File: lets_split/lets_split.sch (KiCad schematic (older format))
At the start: 56 parts, among them P1 USB-rewire, P2 USB_OTG, P3 WS2812-Strip, P4 TRRS jack, SW1 SW_PUSH, SW10 SW_PUSH, SW11 SW_PUSH, SW12 SW_PUSH, SW13 SW_PUSH, SW14 SW_PUSH, SW15 SW_PUSH, SW16 SW_PUSH, SW17 SW_PUSH, SW18 SW_PUSH, SW19 SW_PUSH, SW2 SW_PUSH, SW20 SW_PUSH, SW21 SW_PUSH, SW22 SW_PUSH, SW23 SW_PUSH, SW24 SW_PUSH, SW3 SW_PUSH, SW4 SW_PUSH, SW5 SW_PUSH, SW6 SW_PUSH, SW7 SW_PUSH, SW8 SW_PUSH, SW9 SW_PUSH, U1 ArduinoProMicro

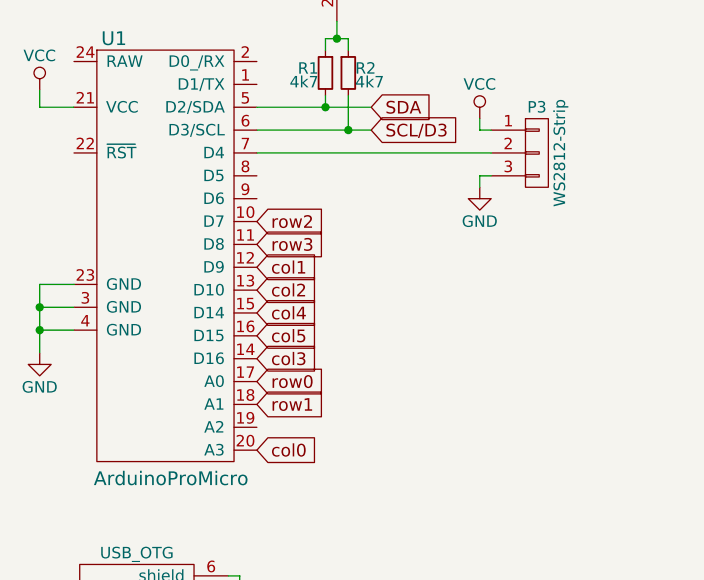
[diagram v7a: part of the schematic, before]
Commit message: Routed board with reversible socket footprint, and mirrored connectors
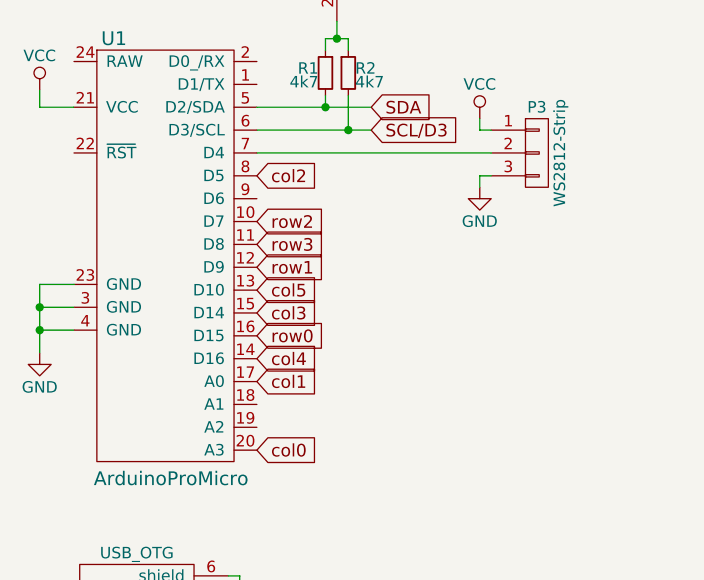
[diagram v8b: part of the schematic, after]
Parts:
- SW1, SW10, SW11, SW12, SW13, SW14, SW15, SW16, SW17, SW18, SW19, SW2, SW20, SW21, SW22, SW23, SW24, SW3, SW4, SW5, SW6, SW7, SW8, SW9: footprint CherryMX:Kailh-socket -> CherryMX:Kailh-socket-mirrorable
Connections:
- net col1: now also U1.17 (A0); no longer U1.12 (D9)
- net col2: now also U1.8 (D5); no longer U1.13 (D10)
- net col3: now also U1.15 (D14); no longer U1.14 (D16)
- net col4: now also U1.14 (D16); no longer U1.15 (D14)
- net col5: now also U1.13 (D10); no longer U1.16 (D15)
- net row0: now also U1.16 (D15); no longer U1.17 (A0)
- net row1: now also U1.12 (D9); no longer U1.18 (A1)
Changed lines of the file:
@@
-EESchema Schematic File Version 2
+EESchema Schematic File Version 3
 LIBS:power
 LIBS:device
-LIBS:transistors
-LIBS:conn
 LIBS:linear
 LIBS:regul
-LIBS:74xx
-LIBS:cmos4000
 LIBS:adc-dac
 LIBS:memory
@@
 LIBS:digital-audio
 LIBS:philips
-LIBS:display
 LIBS:cypress
 LIBS:siliconi
@@
 LIBS:atmel
 LIBS:contrib
-LIBS:valves
 LIBS:8Bit-MCU
 LIBS:lets_split-cache
-EELAYER 25 0
+EELAYER 26 0
 EELAYER END
 $Descr A4 11693 8268
@@
 F 0 "SW1" H 5600 2310 50  0000 C CNN
 F 1 "SW_PUSH" H 5450 2120 50  0000 C CNN
-F 2 "CherryMX:Kailh-socket" H 5450 2200 50  0001 C CNN
+F 2 "CherryMX:Kailh-socket-mirrorable" H 5450 2200 50  0001 C CNN
 F 3 "" H 5450 2200 50  0000 C CNN
 	1    5450 2200
@@
 F 0 "SW2" H 6350 2310 50  0000 C CNN
 F 1 "SW_PUSH" H 6200 2120 50  0000 C CNN
-F 2 "CherryMX:Kailh-socket" H 6200 2200 50  0001 C CNN
+F 2 "CherryMX:Kailh-socket-mirrorable" H 6200 2200 50  0001 C CNN
 F 3 "" H 6200 2200 50  0000 C CNN
 	1    6200 2200
@@
 F 0 "SW3" H 7050 2310 50  0000 C CNN
 F 1 "SW_PUSH" H 6900 2120 50  0000 C CNN
-F 2 "CherryMX:Kailh-socket" H 6900 2200 50  0001 C CNN
+F 2 "CherryMX:Kailh-socket-mirrorable" H 6900 2200 50  0001 C CNN
 F 3 "" H 6900 2200 50  0000 C CNN
 	1    6900 2200
@@
 F 0 "SW4" H 7800 2310 50  0000 C CNN
 F 1 "SW_PUSH" H 7650 2120 50  0000 C CNN
-F 2 "CherryMX:Kailh-socket" H 7650 2200 50  0001 C CNN
+F 2 "CherryMX:Kailh-socket-mirrorable" H 7650 2200 50  0001 C CNN
 F 3 "" H 7650 2200 50  0000 C CNN
 	1    7650 2200
@@
 F 0 "SW5" H 8550 2310 50  0000 C CNN
 F 1 "SW_PUSH" H 8400 2120 50  0000 C CNN
-F 2 "CherryMX:Kailh-socket" H 8400 2200 50  0001 C CNN
+F 2 "CherryMX:Kailh-socket-mirrorable" H 8400 2200 50  0001 C CNN
 F 3 "" H 8400 2200 50  0000 C CNN
 	1    8400 2200
@@
 F 0 "SW6" H 9300 2310 50  0000 C CNN
 F 1 "SW_PUSH" H 9150 2120 50  0000 C CNN
-F 2 "CherryMX:Kailh-socket" H 9150 2200 50  0001 C CNN
+F 2 "CherryMX:Kailh-socket-mirrorable" H 9150 2200 50  0001 C CNN
 F 3 "" H 9150 2200 50  0000 C CNN
 	1    9150 2200
@@
 F 0 "SW7" H 5600 2810 50  0000 C CNN
 F 1 "SW_PUSH" H 5450 2620 50  0000 C CNN
-F 2 "CherryMX:Kailh-socket" H 5450 2700 50  0001 C CNN
+F 2 "CherryMX:Kailh-socket-mirrorable" H 5450 2700 50  0001 C CNN
 F 3 "" H 5450 2700 50  0000 C CNN
 	1    5450 2700
@@
 F 0 "SW8" H 6350 2810 50  0000 C CNN
 F 1 "SW_PUSH" H 6200 2620 50  0000 C CNN
-F 2 "CherryMX:Kailh-socket" H 6200 2700 50  0001 C CNN
+F 2 "CherryMX:Kailh-socket-mirrorable" H 6200 2700 50  0001 C CNN
 F 3 "" H 6200 2700 50  0000 C CNN
 	1    6200 2700
@@
 F 0 "SW9" H 7050 2810 50  0000 C CNN
 F 1 "SW_PUSH" H 6900 2620 50  0000 C CNN
-F 2 "CherryMX:Kailh-socket" H 6900 2700 50  0001 C CNN
+F 2 "CherryMX:Kailh-socket-mirrorable" H 6900 2700 50  0001 C CNN
 F 3 "" H 6900 2700 50  0000 C CNN
 	1    6900 2700
@@
 F 0 "SW10" H 7800 2810 50  0000 C CNN
 F 1 "SW_PUSH" H 7650 2620 50  0000 C CNN
-F 2 "CherryMX:Kailh-socket" H 7650 2700 50  0001 C CNN
+F 2 "CherryMX:Kailh-socket-mirrorable" H 7650 2700 50  0001 C CNN
 F 3 "" H 7650 2700 50  0000 C CNN
 	1    7650 2700
@@
 F 0 "SW11" H 8550 2810 50  0000 C CNN
 F 1 "SW_PUSH" H 8400 2620 50  0000 C CNN
-F 2 "CherryMX:Kailh-socket" H 8400 2700 50  0001 C CNN
+F 2 "CherryMX:Kailh-socket-mirrorable" H 8400 2700 50  0001 C CNN
 F 3 "" H 8400 2700 50  0000 C CNN
 	1    8400 2700
@@
 F 0 "SW12" H 9300 2810 50  0000 C CNN
 F 1 "SW_PUSH" H 9150 2620 50  0000 C CNN
-F 2 "CherryMX:Kailh-socket" H 9150 2700 50  0001 C CNN
+F 2 "CherryMX:Kailh-socket-mirrorable" H 9150 2700 50  0001 C CNN
 F 3 "" H 9150 2700 50  0000 C CNN
 	1    9150 2700
@@
 F 0 "SW13" H 5600 3310 50  0000 C CNN
 F 1 "SW_PUSH" H 5450 3120 50  0000 C CNN
-F 2 "CherryMX:Kailh-socket" H 5450 3200 50  0001 C CNN
+F 2 "CherryMX:Kailh-socket-mirrorable" H 5450 3200 50  0001 C CNN
 F 3 "" H 5450 3200 50  0000 C CNN
 	1    5450 3200
@@
 F 0 "SW14" H 6350 3310 50  0000 C CNN
 F 1 "SW_PUSH" H 6200 3120 50  0000 C CNN
-F 2 "CherryMX:Kailh-socket" H 6200 3200 50  0001 C CNN
+F 2 "CherryMX:Kailh-socket-mirrorable" H 6200 3200 50  0001 C CNN
 F 3 "" H 6200 3200 50  0000 C CNN
 	1    6200 3200
@@
 F 0 "SW15" H 7050 3310 50  0000 C CNN
 F 1 "SW_PUSH" H 6900 3120 50  0000 C CNN
-F 2 "CherryMX:Kailh-socket" H 6900 3200 50  0001 C CNN
+F 2 "CherryMX:Kailh-socket-mirrorable" H 6900 3200 50  0001 C CNN
 F 3 "" H 6900 3200 50  0000 C CNN
 	1    6900 3200
@@
 F 0 "SW16" H 7800 3310 50  0000 C CNN
 F 1 "SW_PUSH" H 7650 3120 50  0000 C CNN
-F 2 "CherryMX:Kailh-socket" H 7650 3200 50  0001 C CNN
+F 2 "CherryMX:Kailh-socket-mirrorable" H 7650 3200 50  0001 C CNN
 F 3 "" H 7650 3200 50  0000 C CNN
 	1    7650 3200
@@
 F 0 "SW17" H 8550 3310 50  0000 C CNN
 F 1 "SW_PUSH" H 8400 3120 50  0000 C CNN
-F 2 "CherryMX:Kailh-socket" H 8400 3200 50  0001 C CNN
+F 2 "CherryMX:Kailh-socket-mirrorable" H 8400 3200 50  0001 C CNN
 F 3 "" H 8400 3200 50  0000 C CNN
 	1    8400 3200
@@
 F 0 "SW18" H 9300 3310 50  0000 C CNN
 F 1 "SW_PUSH" H 9150 3120 50  0000 C CNN
-F 2 "CherryMX:Kailh-socket" H 9150 3200 50  0001 C CNN
+F 2 "CherryMX:Kailh-socket-mirrorable" H 9150 3200 50  0001 C CNN
 F 3 "" H 9150 3200 50  0000 C CNN
 	1    9150 3200
@@
 F 0 "SW19" H 5600 3810 50  0000 C CNN
 F 1 "SW_PUSH" H 5450 3620 50  0000 C CNN
-F 2 "CherryMX:Kailh-socket" H 5450 3700 50  0001 C CNN
+F 2 "CherryMX:Kailh-socket-mirrorable" H 5450 3700 50  0001 C CNN
 F 3 "" H 5450 3700 50  0000 C CNN
 	1    5450 3700
@@
 F 0 "SW20" H 6350 3810 50  0000 C CNN
 F 1 "SW_PUSH" H 6200 3620 50  0000 C CNN
-F 2 "CherryMX:Kailh-socket" H 6200 3700 50  0001 C CNN
+F 2 "CherryMX:Kailh-socket-mirrorable" H 6200 3700 50  0001 C CNN
 F 3 "" H 6200 3700 50  0000 C CNN
 	1    6200 3700
@@
 F 0 "SW21" H 7050 3810 50  0000 C CNN
 F 1 "SW_PUSH" H 6900 3620 50  0000 C CNN
-F 2 "CherryMX:Kailh-socket" H 6900 3700 50  0001 C CNN
+F 2 "CherryMX:Kailh-socket-mirrorable" H 6900 3700 50  0001 C CNN
 F 3 "" H 6900 3700 50  0000 C CNN
 	1    6900 3700
@@
 F 0 "SW22" H 7800 3810 50  0000 C CNN
 F 1 "SW_PUSH" H 7650 3620 50  0000 C CNN
-F 2 "CherryMX:Kailh-socket" H 7650 3700 50  0001 C CNN
+F 2 "CherryMX:Kailh-socket-mirrorable" H 7650 3700 50  0001 C CNN
 F 3 "" H 7650 3700 50  0000 C CNN
 	1    7650 3700
@@
 F 0 "SW23" H 8550 3810 50  0000 C CNN
 F 1 "SW_PUSH" H 8400 3620 50  0000 C CNN
-F 2 "CherryMX:Kailh-socket" H 8400 3700 50  0001 C CNN
+F 2 "CherryMX:Kailh-socket-mirrorable" H 8400 3700 50  0001 C CNN
 F 3 "" H 8400 3700 50  0000 C CNN
 	1    8400 3700
@@
 F 0 "SW24" H 9300 3810 50  0000 C CNN
 F 1 "SW_PUSH" H 9150 3620 50  0000 C CNN
-F 2 "CherryMX:Kailh-socket" H 9150 3700 50  0001 C CNN
+F 2 "CherryMX:Kailh-socket-mirrorable" H 9150 3700 50  0001 C CNN
 F 3 "" H 9150 3700 50  0000 C CNN
 	1    9150 3700
@@
 Text GLabel 2350 3475 2    55   Input ~ 0
 col0
-Text GLabel 2350 2675 2    55   Input ~ 0
+Text GLabel 2350 3175 2    55   Input ~ 0
 col1
+Text GLabel 2350 2275 2    55   Input ~ 0
+col2
+Text GLabel 2350 2875 2    55   Input ~ 0
+col3
+Text GLabel 2350 3075 2    55   Input ~ 0
+col4
 Text GLabel 2350 2775 2    55   Input ~ 0
-col2
-Text GLabel 2350 3075 2    55   Input ~ 0
-col3
-Text GLabel 2350 2875 2    55   Input ~ 0
-col4
-Text GLabel 2350 2975 2    55   Input ~ 0
 col5
 Text GLabel 2350 2575 2    55   Input ~ 0
@@
 Text GLabel 2350 2475 2    55   Input ~ 0
 row2
-Text GLabel 2350 3275 2    55   Input ~ 0
+Text GLabel 2350 2675 2    55   Input ~ 0
 row1
-Text GLabel 2350 3175 2    55   Input ~ 0
+Text GLabel 2350 2975 2    55   Input ~ 0
 row0
 $Comp
